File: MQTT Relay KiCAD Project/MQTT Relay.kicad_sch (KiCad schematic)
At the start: 18 parts, among them J1 Power, J2 Temp 0, J3 Input 0, J4 Input 1, J5 Relay 0, J6 Relay 1, J7 Line Out, SW1 SW_Push, SW2 SW_Push, SW3 SW_Push, U1 SSD1306_128x32, U2 DFPlayer_Module

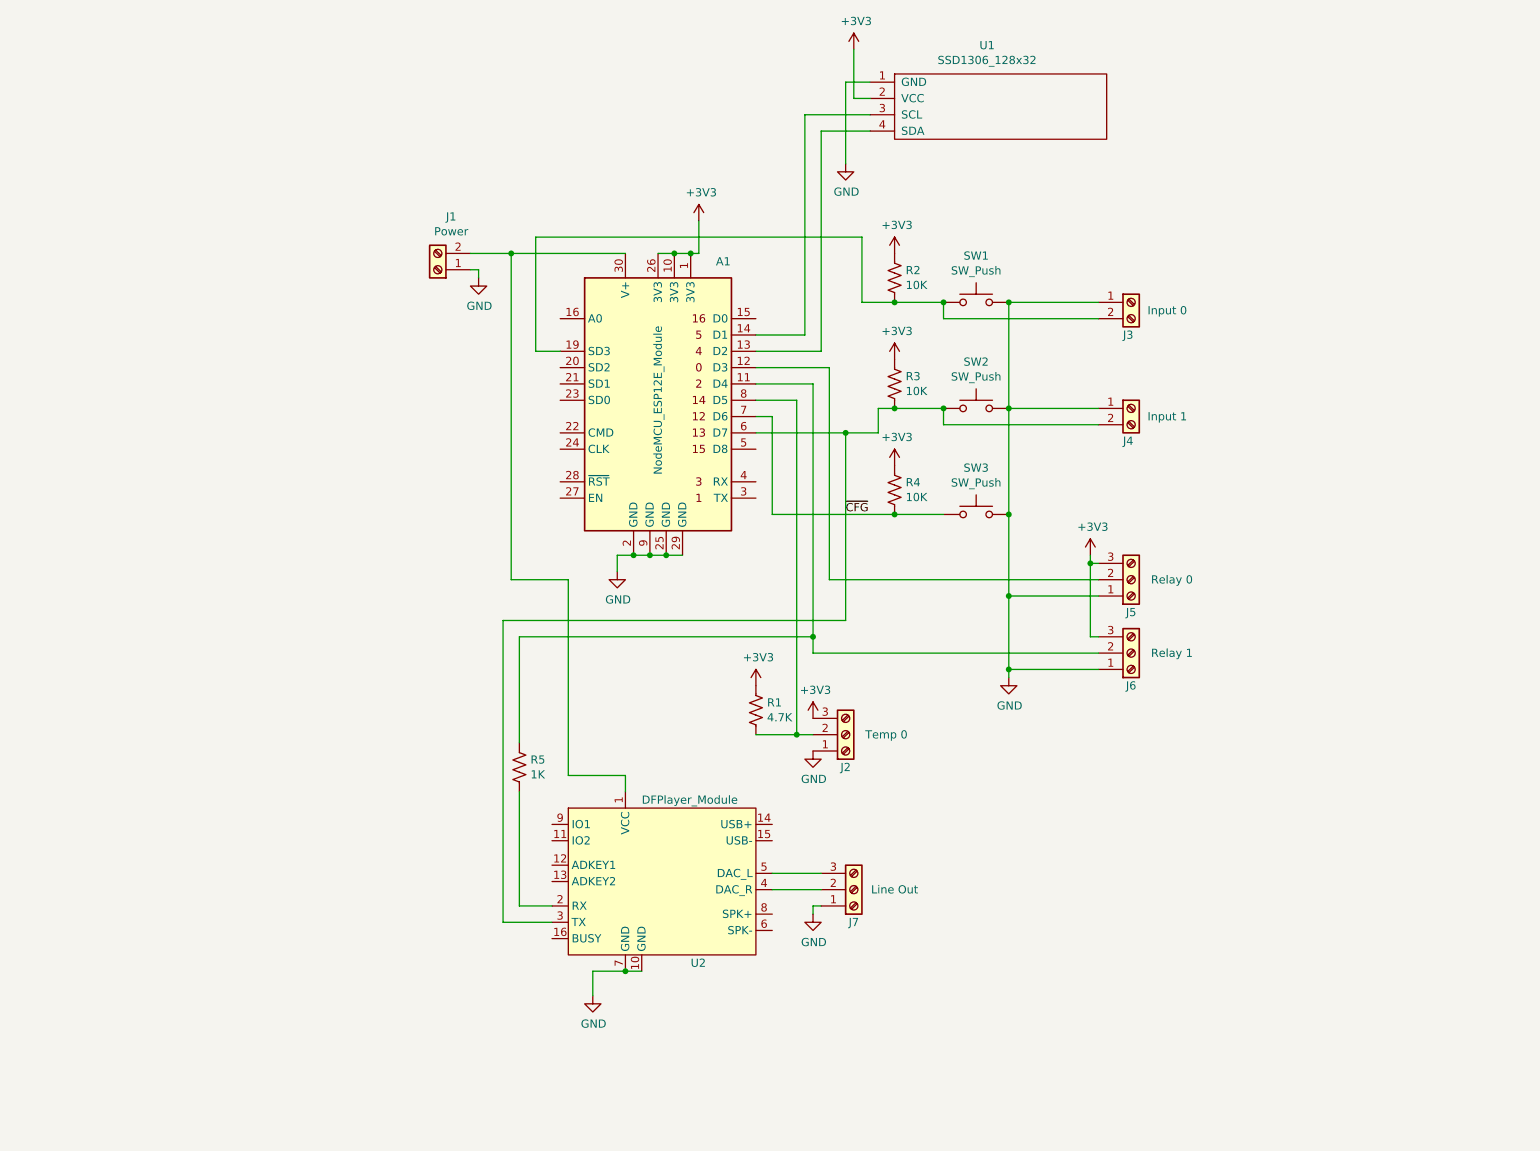
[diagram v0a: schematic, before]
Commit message: Version 3.0 Board
Integrated relays and SMD
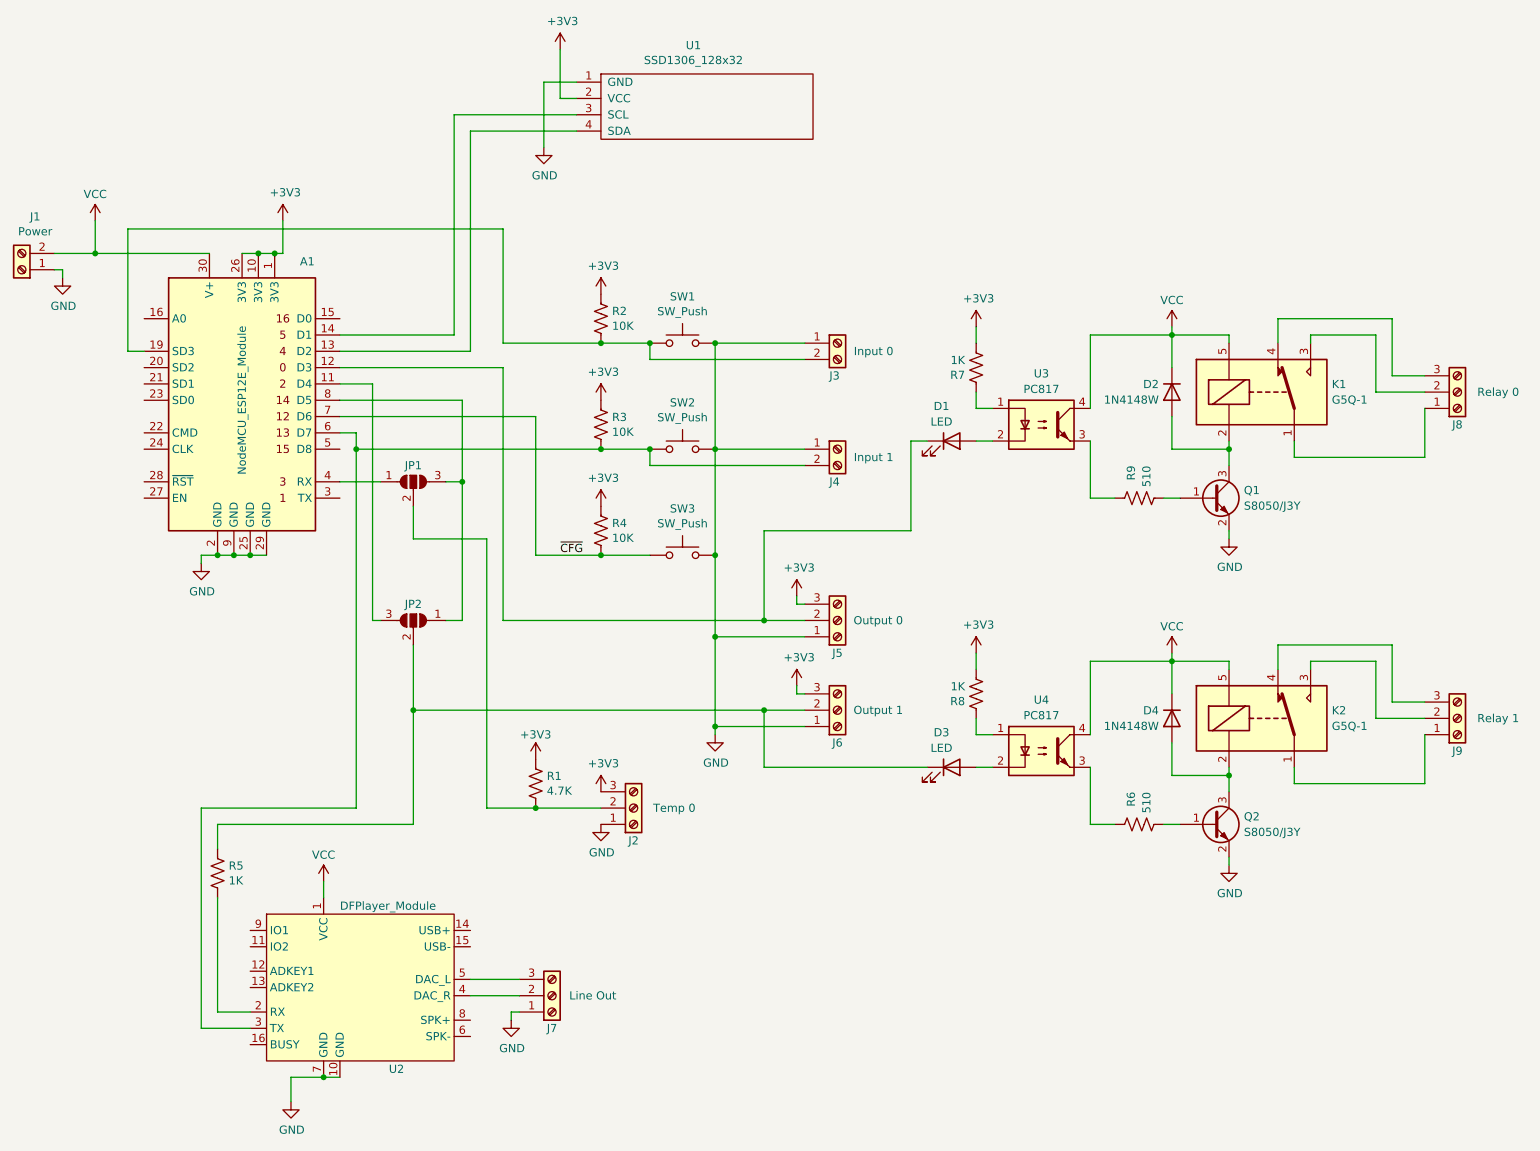
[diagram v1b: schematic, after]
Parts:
- added D1, D3: LED, LED_SMD:LED_0603_1608Metric_Pad1.05x0.95mm_HandSolder, symbol Device:LED
- added D2, D4: 1N4148W, Diode_SMD:D_SOD-123, symbol Diode:1N4148W
- added J8: Relay 0, TerminalBlock_Phoenix:TerminalBlock_Phoenix_MPT-0,5-3-2.54_1x03_P2.54mm_Horizontal, symbol Connector:Screw_Terminal_01x03
- added J9: Relay 1, TerminalBlock_Phoenix:TerminalBlock_Phoenix_MPT-0,5-3-2.54_1x03_P2.54mm_Horizontal, symbol Connector:Screw_Terminal_01x03
- added JP1: T-0, Jumper:SolderJumper-3_P1.3mm_Open_Pad1.0x1.5mm_NumberLabels, symbol Jumper:SolderJumper_3_Open
- added JP2: R-1, Jumper:SolderJumper-3_P1.3mm_Open_Pad1.0x1.5mm_NumberLabels, symbol Jumper:SolderJumper_3_Open
- added K1, K2: G5Q-1, Relay_THT:Relay_SPDT_SANYOU_SRD_Series_Form_C, symbol Relay:G5Q-1
- added Q1, Q2: S8050/J3Y, Package_TO_SOT_SMD:SOT-23-3, symbol Transistor_BJT:J3Y
- added R6, R9: 510, Resistor_SMD:R_1206_3216Metric_Pad1.30x1.75mm_HandSolder, symbol Device:R_US
- added R7, R8: 1K, Resistor_SMD:R_1206_3216Metric_Pad1.30x1.75mm_HandSolder, symbol Device:R_US
- added U3, U4: PC817, Package_DIP:DIP-4_W7.62mm, symbol Isolator:PC817
- J5: value Relay 0 -> Output 0
- J6: value Relay 1 -> Output 1
- R1, R2, R3, R4, R5: footprint Resistor_THT:R_Axial_DIN0207_L6.3mm_D2.5mm_P10.16mm_Horizontal -> Resistor_SMD:R_1206_3216Metric_Pad1.30x1.75mm_HandSolder
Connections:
- net +3V3: now also R7.2, R8.2
- net GND: now also Q1.2 (E), Q2.2 (E)
- net ~{CFG}: no longer A1.6 (D7), J4.2 (Pin_2), R3.2, SW2.1, U2.3 (TX)
- net at J6.2 (Pin_2), R5.1: now also D3.1 (K), JP2.2 (C); no longer A1.11 (D4)
- net at A1.12 (D3), J5.2 (Pin_2): now also D1.1 (K)
- net VCC: now reaches A1.30 (V+), J1.2 (Pin_2), U2.1 (VCC)
- net VCC: now also D2.1 (K), D4.1 (K), K1.5, K2.5, U3.4, U4.4
- net at A1.4 (RX): now also JP1.1 (A)
- net at J2.2 (Pin_2), R1.2: now also JP1.2 (C); no longer A1.8 (D5)
- new net: A1.11 (D4), JP2.3 (B)
- new net: A1.6 (D7), J4.2 (Pin_2), R3.2, SW2.1, U2.3 (TX)
- new net: A1.8 (D5), JP1.3 (B), JP2.1 (A)
- new net: D3.2 (A), U4.2
- new net: J9.1 (Pin_1), K2.1
- new net: J9.2 (Pin_2), K2.3
- new net: J9.3 (Pin_3), K2.4
- new net: R7.1, U3.1
- new net: D1.2 (A), U3.2
- new net: R9.1, U3.3
- new net: J8.1 (Pin_1), K1.1
- new net: D2.2 (A), K1.2, Q1.3 (C)
- new net: J8.2 (Pin_2), K1.3
- new net: J8.3 (Pin_3), K1.4
- new net: Q1.1 (B), R9.2
- new net: Q2.1 (B), R6.2
- new net: D4.2 (A), K2.2, Q2.3 (C)
- new net: R8.1, U4.1
- new net: R6.1, U4.3
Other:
- moved on the sheet: A1, J1, J2, J3, J4, J5, J6, J7, R1, R2, R3, R4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

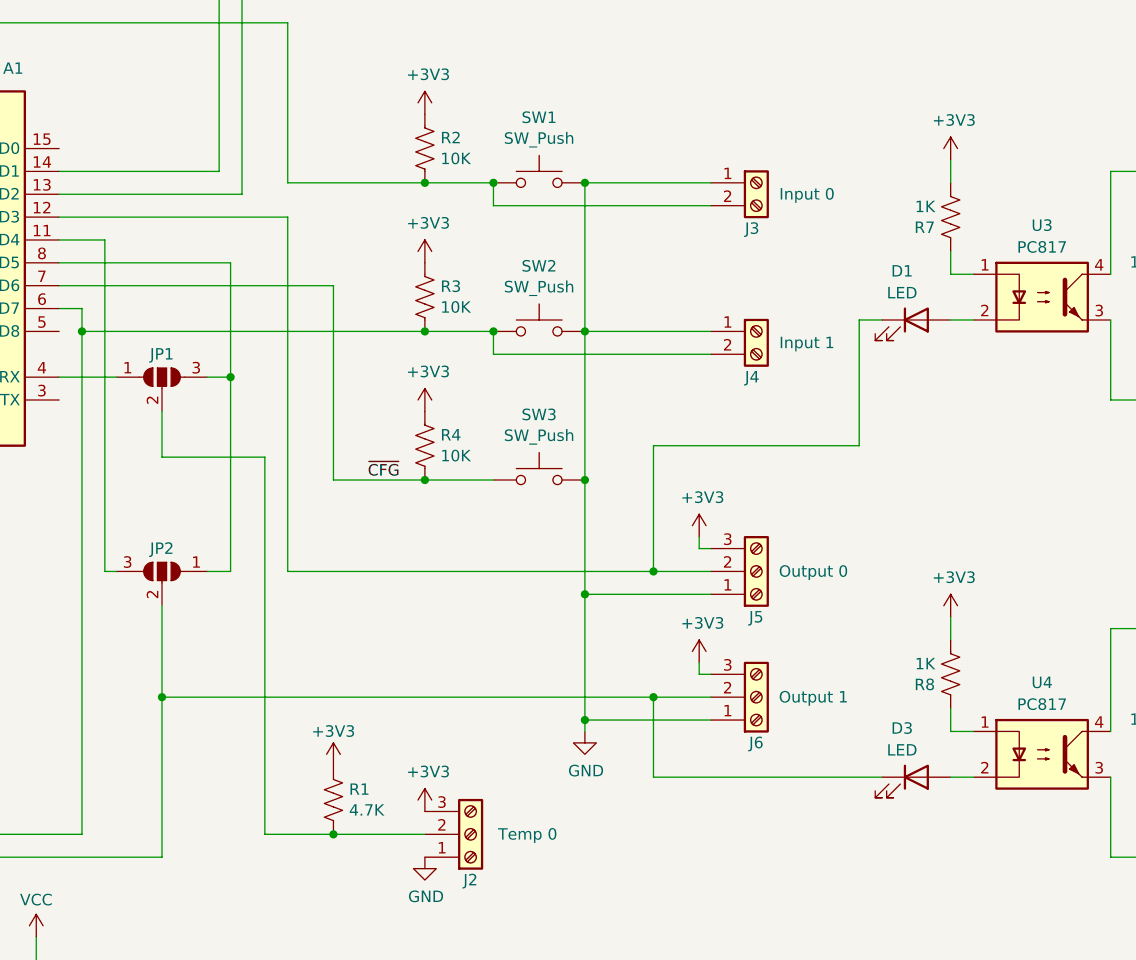
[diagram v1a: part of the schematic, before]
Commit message: Added Relays onBoard
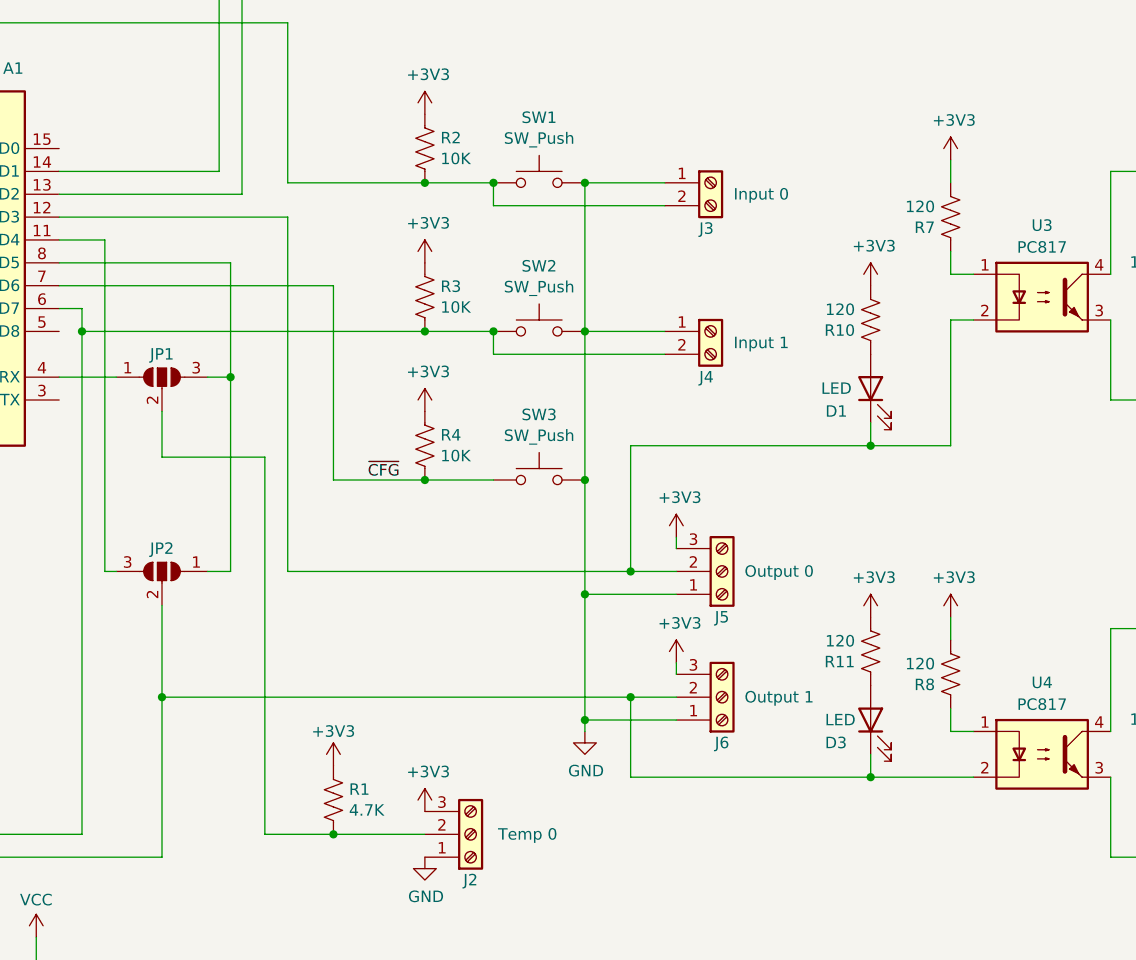
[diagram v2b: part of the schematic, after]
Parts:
- added R10, R11: 120, Resistor_SMD:R_1206_3216Metric_Pad1.30x1.75mm_HandSolder, symbol Device:R_US
- D1, D3: footprint LED_SMD:LED_0603_1608Metric_Pad1.05x0.95mm_HandSolder -> LED_SMD:LED_1206_3216Metric_Pad1.42x1.75mm_HandSolder
- R7, R8: value 1K -> 120
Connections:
- net +3V3: now also R10.2, R11.2
- net at A1.12 (D3), D1.1 (K), J5.2 (Pin_2): now also U3.2
- net at D3.1 (K), J6.2 (Pin_2), JP2.2 (C)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: now also U4.2
- net at D3.2 (A): now also R11.1; no longer U4.2
- net at D1.2 (A): now also R10.1; no longer U3.2
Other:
- moved on the sheet: J3, J4, J5, J6
